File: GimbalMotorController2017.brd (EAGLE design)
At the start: 112.4 x 80 mm, 137 parts, among them J3 APP_2POS_CONFIG5V_HORIZ, Q1 MOSFET-NCHANNELFQP30N06L, Q2 MOSFET-NCHANNELFQP30N06L, Q3 MOSFET-NCHANNELFQP30N06L, Q4 MOSFET-NCHANNELFQP30N06L, Q7 MOSFET-PCHANNEL, Q8 MOSFET-PCHANNEL, Q9 MOSFET-NCHANNELAO3404A, U1 NUP4201MR6, U2 MAX3232D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

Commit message: added CSD18533Q5A fets to Phase B in place of the previously used fets
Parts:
- removed Q3, Q4: MOSFET-NCHANNELFQP30N06L, SparkFun-DiscreteSemi:TO220V
- added U5, U6: CSD18533Q5A, CSD18533:DQJ8
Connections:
- net N$14: now also U6.4; no longer Q3.1
- net N$15: now also U5.4; no longer Q4.1
- net PVDD: now also U6.8; no longer Q3.2
- net SH_B: now also U5.8, U6.3; no longer Q3.3, Q4.2
- net SL_B: now also U5.3; no longer Q4.3
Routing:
- net N$14: track 16.4 -> 12.5 mm
- net N$15: track 10.7 -> 7.85 mm
- net SH_B: track 108.3 -> 106.8 mm
- net GND: track 16.8 -> 15.6 mm
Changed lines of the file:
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@@
 <attribute name="PROD_ID" value="TRANS-10060" x="40.513" y="58.89625" size="1.778" layer="28" rot="MR180" display="off"/>
-</element>
-<element name="Q3" library="SparkFun-DiscreteSemi" package="TO220V" value="MOSFET-NCHANNELFQP30N06L" x="56.388" y="58.89625" smashed="yes" rot="MR180">
-<attribute name="NAME" x="59.944" y="55.46725" size="0.6096" layer="26" ratio="10" rot="MR180"/>
-<attribute name="PROD_ID" value="TRANS-10060" x="56.388" y="58.89625" size="1.778" layer="28" rot="MR180" display="off"/>
-</element>
-<element name="Q4" library="SparkFun-DiscreteSemi" package="TO220V" value="MOSFET-NCHANNELFQP30N06L" x="70.993" y="58.89625" smashed="yes" rot="MR180">
-<attribute name="NAME" x="74.549" y="55.46725" size="0.6096" layer="26" ratio="10" rot="MR180"/>
-<attribute name="PROD_ID" value="TRANS-10060" x="70.993" y="58.89625" size="1.778" layer="28" rot="MR180" display="off"/>
 </element>
 <element name="Q7" library="SparkFun-DiscreteSemi" package="SOT23-3" value="MOSFET-PCHANNEL" x="99.21875" y="43.815" smashed="yes" rot="R270">
@@
 <attribute name="MANUFACTURER_PART_NUMBER" value="CSD18533Q5A" x="-27.94" y="-52.578" size="1.778" layer="27" display="off"/>
 <attribute name="VENDOR" value="Texas Instruments" x="-27.94" y="-52.578" size="1.778" layer="27" display="off"/>
+</element>
+<element name="U5" library="CSD18533" package="DQJ8" value="CSD18533Q5A" x="-27.94" y="-58.674">
+<attribute name="MANUFACTURER_PART_NUMBER" value="CSD18533Q5A" x="-27.94" y="-58.674" size="1.778" layer="27" display="off"/>
+<attribute name="VENDOR" value="Texas Instruments" x="-27.94" y="-58.674" size="1.778" layer="27" display="off"/>
+</element>
+<element name="U6" library="CSD18533" package="DQJ8" value="CSD18533Q5A" x="-27.94" y="-64.77">
+<attribute name="MANUFACTURER_PART_NUMBER" value="CSD18533Q5A" x="-27.94" y="-64.77" size="1.778" layer="27" display="off"/>
+<attribute name="VENDOR" value="Texas Instruments" x="-27.94" y="-64.77" size="1.778" layer="27" display="off"/>
 </element>
 </elements>
@@
 <wire x1="87.4395" y1="66.675" x2="85.88075" y2="66.675" width="0.508" layer="1"/>
 <wire x1="85.88075" y1="66.675" x2="85.852" y2="66.64625" width="0.508" layer="1"/>
-<contactref element="SH1" pad="2"/>
 <contactref element="C24" pad="2"/>
 <contactref element="R18" pad="1"/>
@@
 <via x="45.4025" y="41.62425" extent="1-16" drill="0.381" shape="square"/>
 <wire x1="47.371" y1="62.47765" x2="47.371" y2="63.66175" width="0.3048" layer="16"/>
-<wire x1="77.851" y1="62.47765" x2="77.851" y2="63.66175" width="0.3048" layer="16"/>
 <contactref element="U2" pad="15"/>
 <contactref element="C46" pad="2"/>
@@
 </polygon>
 <contactref element="U4" pad="3"/>
+<contactref element="SH1" pad="2"/>
 <wire x1="108.204" y1="54.61" x2="101.847" y2="63.3095" width="0" layer="19" extent="16-16"/>
 <wire x1="104.66875" y1="47.625" x2="108.204" y2="54.61" width="0" layer="19" extent="1-1"/>
@@
 <wire x1="80.04175" y1="63.0665" x2="84.2645" y2="66.675" width="0" layer="19" extent="16-16"/>
 <wire x1="77.851" y1="63.66175" x2="80.04175" y2="63.0665" width="0" layer="19" extent="16-16"/>
+<wire x1="77.851" y1="62.47765" x2="77.851" y2="63.66175" width="0" layer="19" extent="16-16"/>
 <wire x1="78.74" y1="68.58" x2="77.851" y2="63.66175" width="0" layer="19" extent="16-16"/>
 <wire x1="23.3045" y1="66.675" x2="10.16" y2="76.2" width="0" layer="19" extent="1-1"/>
@@
 <contactref element="Q1" pad="2"/>
 <contactref element="C19" pad="1"/>
-<contactref element="Q3" pad="2"/>
 <contactref element="C22" pad="1"/>
 <contactref element="C25" pad="1"/>
@@
 <contactref element="C37" pad="1"/>
 <contactref element="U3" pad="8"/>
-<wire x1="56.388" y1="58.89625" x2="85.852" y2="63.84625" width="0" layer="19" extent="1-1"/>
-<wire x1="55.372" y1="63.84625" x2="56.388" y2="58.89625" width="0" layer="19" extent="1-1"/>
-<wire x1="62.5585" y1="39.0525" x2="56.388" y2="58.89625" width="0" layer="19" extent="1-1"/>
+<contactref element="U6" pad="8"/>
+<wire x1="55.372" y1="63.84625" x2="85.852" y2="63.84625" width="0" layer="19" extent="1-1"/>
+<wire x1="62.5585" y1="39.0525" x2="55.372" y2="63.84625" width="0" layer="19" extent="1-1"/>
 <wire x1="54.55" y1="18.65" x2="54.55" y2="30.65" width="0" layer="19" extent="1-1"/>
 <wire x1="54.55" y1="17.61775" x2="54.55" y2="18.65" width="0" layer="19" extent="1-1"/>
@@
 <wire x1="22.86" y1="19.812" x2="23.84425" y2="44.73575" width="0" layer="19" extent="1-1"/>
 <wire x1="-25.204928125" y1="-44.577" x2="22.86" y2="19.812" width="0" layer="19" extent="1-1"/>
+<wire x1="-25.204928125" y1="-62.865" x2="-25.204928125" y2="-44.577" width="0" layer="19" extent="1-1"/>
 </signal>
 <signal name="GL_C">
@@
 <signal name="SL_B">
 <contactref element="U$1" pad="39"/>
-<contactref element="Q4" pad="3"/>
 <contactref element="C24" pad="1"/>
 <contactref element="U$1" pad="31"/>
@@
 <wire x1="59.2455" y1="19.14525" x2="59.2455" y2="20.66925" width="0.3048" layer="15"/>
 <contactref element="D10" pad="A"/>
+<contactref element="U5" pad="3"/>
+<wire x1="77.851" y1="60.86175" x2="80.04175" y2="61.2665" width="0" layer="19" extent="16-16"/>
+<wire x1="78.74" y1="57.15" x2="77.851" y2="60.86175" width="0" layer="19" extent="16-16"/>
+<wire x1="74.302" y1="56.388" x2="78.4225" y2="56.8325" width="0" layer="19" extent="16-16"/>
+<wire x1="-30.675071875" y1="-59.309" x2="54.55" y2="19.65" width="0" layer="19" extent="1-1"/>
 </signal>
 <signal name="GL_B">
@@
 <contactref element="C12" pad="2"/>
 <contactref element="U$1" pad="41"/>
-<contactref element="Q3" pad="3"/>
-<contactref element="Q4" pad="2"/>
 <contactref element="R19" pad="1"/>
 <contactref element="U$6" pad="P$1"/>
@@
 <wire x1="60.205" y1="56.1975" x2="60.0145" y2="56.388" width="0.3048" layer="16"/>
 <wire x1="60.0145" y1="56.388" x2="60.0145" y2="57.80975" width="0.3048" layer="16"/>
-<wire x1="60.0145" y1="57.80975" x2="58.928" y2="58.89625" width="0.3048" layer="16"/>
 <wire x1="71.4265" y1="24.59525" x2="71.4265" y2="28.1415" width="0.3048" layer="1"/>
 <wire x1="71.4265" y1="28.1415" x2="68.072" y2="31.496" width="0.3048" layer="1"/>
@@
 <wire x1="50.292" y1="54.61" x2="56.134" y2="54.61" width="0.3048" layer="1"/>
 <wire x1="56.134" y1="54.61" x2="58.674" y2="57.15" width="0.3048" layer="1"/>
+<contactref element="U5" pad="8"/>
+<contactref element="U6" pad="3"/>
+<wire x1="60.0145" y1="57.80975" x2="63.65875" y2="60.706" width="0" layer="19" extent="16-16"/>
+<wire x1="58.674" y1="57.15" x2="60.0145" y2="57.80975" width="0" layer="19" extent="1-16"/>
+<wire x1="-25.204928125" y1="-56.769" x2="54.55" y2="24.65" width="0" layer="19" extent="1-1"/>
+<wire x1="-30.675071875" y1="-65.405" x2="-25.204928125" y2="-56.769" width="0" layer="19" extent="1-1"/>
 </signal>
 <signal name="SL_A">
@@
 </signal>
 <signal name="N$14">
-<contactref element="Q3" pad="1"/>
 <contactref element="R16" pad="1"/>
 <contactref element="D11" pad="C"/>
 <contactref element="U$16" pad="P$1"/>
 <wire x1="53.61475" y1="55.88" x2="53.61475" y2="58.663" width="0.508" layer="16"/>
-<wire x1="53.61475" y1="58.663" x2="53.848" y2="58.89625" width="0.508" layer="16"/>
 <wire x1="57.7145" y1="56.388" x2="56.35625" y2="56.388" width="0.3048" layer="16"/>
-<wire x1="56.35625" y1="56.388" x2="53.848" y2="58.89625" width="0.3048" layer="16"/>
 <wire x1="45.974" y1="54.61" x2="47.244" y2="55.88" width="0.3048" layer="1"/>
 <wire x1="47.244" y1="55.88" x2="52.324" y2="55.88" width="0.3048" layer="1"/>
@@
 <wire x1="52.578" y1="56.134" x2="53.23375" y2="56.134" width="0.3048" layer="16"/>
 <wire x1="53.23375" y1="56.134" x2="53.61475" y2="55.88" width="0.3048" layer="16"/>
+<contactref element="U6" pad="4"/>
+<wire x1="53.61475" y1="55.88" x2="56.35625" y2="56.388" width="0" layer="19" extent="16-16"/>
+<wire x1="-30.675071875" y1="-66.675" x2="45.974" y2="54.61" width="0" layer="19" extent="1-1"/>
 </signal>
 <signal name="N$15">
-<contactref element="Q4" pad="1"/>
 <contactref element="R17" pad="1"/>
 <contactref element="D10" pad="C"/>
@@
 <wire x1="72.002" y1="56.388" x2="71.494" y2="56.896" width="0.508" layer="16"/>
 <wire x1="71.494" y1="56.896" x2="70.45325" y2="56.896" width="0.508" layer="16"/>
-<wire x1="70.45325" y1="56.896" x2="68.453" y2="58.89625" width="0.508" layer="16"/>
 <wire x1="77.089" y1="53.95425" x2="76.43325" y2="54.61" width="0.508" layer="16"/>
 <wire x1="76.43325" y1="54.61" x2="75.184" y2="54.61" width="0.508" layer="16"/>
+<contactref element="U5" pad="4"/>
+<wire x1="-30.675071875" y1="-60.579" x2="70.45325" y2="56.896" width="0" layer="19" extent="1-16"/>
 </signal>
 <signal name="N$17">

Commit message: added CSD18533Q5A fets to Phase A in place of previously used fets. Cleaned up schematic.
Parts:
- removed Q1, Q2: MOSFET-NCHANNELFQP30N06L, SparkFun-DiscreteSemi:TO220V
- added U7, U8: CSD18533Q5A, CSD18533:DQJ8
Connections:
- net N$13: now also U8.4; no longer Q1.1
- net N$16: now also U7.4; no longer Q2.1
- net PVDD: now also U8.8; no longer Q1.2
- net SH_A: now also U7.8, U8.3; no longer Q1.3, Q2.2
- net SL_A: now also U7.3; no longer Q2.3
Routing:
- net SH_A: track 101.6 -> 98.3 mm
- net N$16: track 13.1 -> 10.6 mm
- net GND: track 15.6 -> 14.4 mm
- net N$13: track 7.82 -> 7.01 mm

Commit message: adjusted phase resistor values for 12v to 3.3v voltage divider
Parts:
- R14, R19, R24: value 46.4k -> 13.2k
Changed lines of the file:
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@@
 <element name="R11" library="SparkFun-Passives" package="0805" value="10" x="22.7965" y="54.9275" rot="MR270"/>
 <element name="R12" library="SparkFun-Passives" package="0805" value="10" x="40.16375" y="53.49875" rot="MR180"/>
-<element name="R14" library="SparkFun-Passives" package="0805" value="46.4k" x="56.8325" y="39.0525" smashed="yes" rot="R180">
+<element name="R14" library="SparkFun-Passives" package="0805" value="13.2k" x="56.8325" y="39.0525" smashed="yes" rot="R180">
 <attribute name="NAME" x="57.5945" y="40.513" size="0.6096" layer="25" rot="R180"/>
 <attribute name="VALUE" x="57.8485" y="40.4495" size="0.4064" layer="27" rot="R180"/>
@@
 <attribute name="VALUE" x="78.486" y="54.07025" size="0.4064" layer="28" rot="MR270"/>
 </element>
-<element name="R19" library="SparkFun-Passives" package="0805" value="46.4k" x="52.2605" y="39.0525" smashed="yes">
+<element name="R19" library="SparkFun-Passives" package="0805" value="13.2k" x="52.2605" y="39.0525" smashed="yes">
 <attribute name="NAME" x="52.0065" y="37.592" size="0.6096" layer="25"/>
 <attribute name="VALUE" x="51.2445" y="37.6555" size="0.4064" layer="27"/>
@@
 <attribute name="VALUE" x="28.60675" y="45.847" size="0.4064" layer="27" rot="R270"/>
 </element>
-<element name="R24" library="SparkFun-Passives" package="0805" value="46.4k" x="47.4345" y="39.0525" smashed="yes">
+<element name="R24" library="SparkFun-Passives" package="0805" value="13.2k" x="47.4345" y="39.0525" smashed="yes">
 <attribute name="NAME" x="47.4345" y="37.592" size="0.6096" layer="25"/>
 <attribute name="VALUE" x="46.4185" y="37.6555" size="0.4064" layer="27"/>

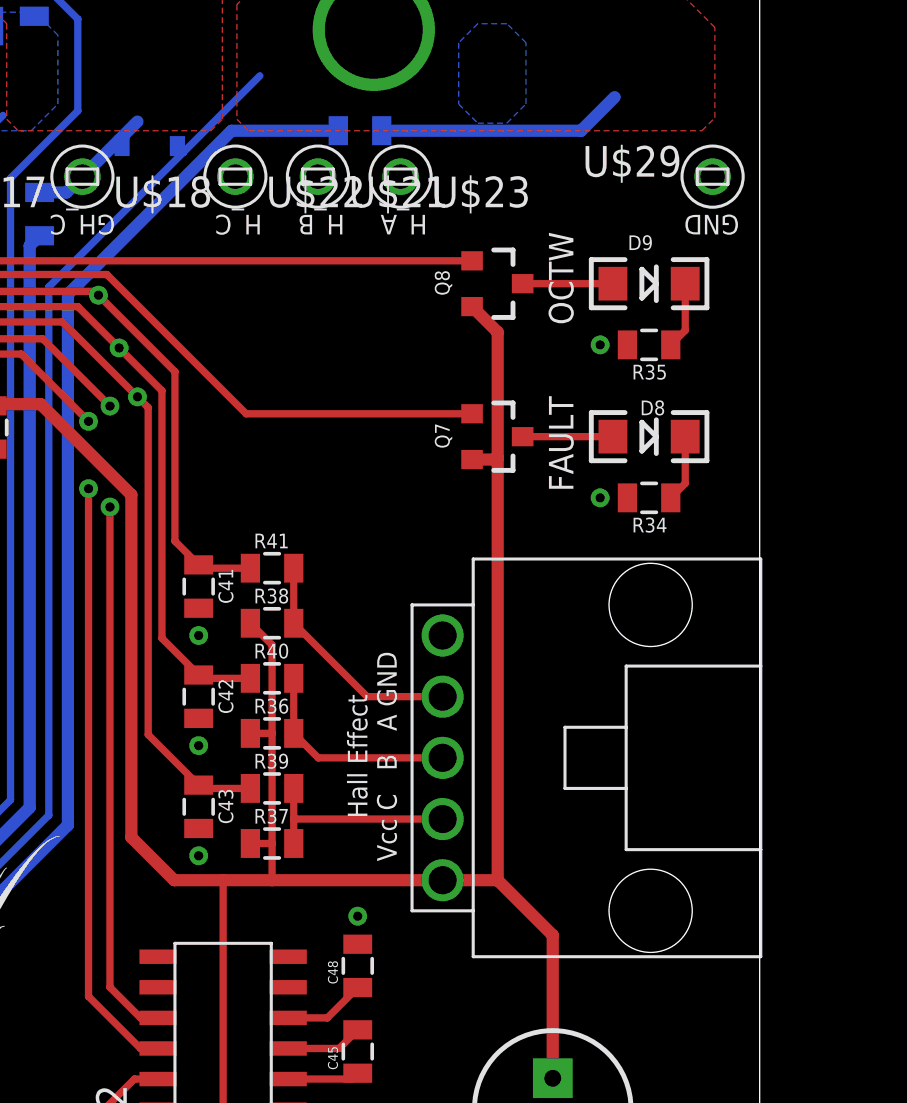
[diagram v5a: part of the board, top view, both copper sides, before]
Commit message: removed hall effect sensor connector
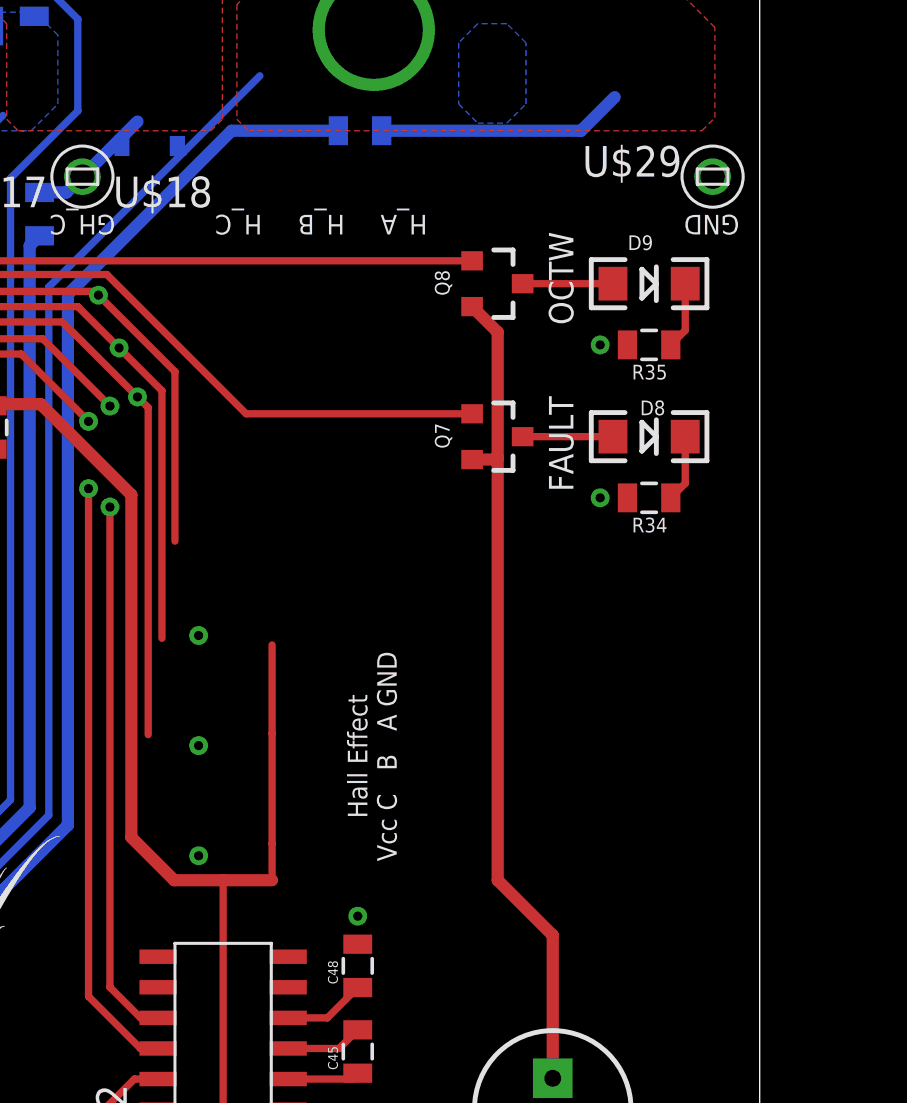
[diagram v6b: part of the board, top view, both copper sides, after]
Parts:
- removed C41, C42, C43: .015u, SparkFun-Passives:0805
- removed R36, R37, R38: 10k, SparkFun-Passives:0805
- removed R39, R40, R41: 10, SparkFun-Passives:0805
- removed U$21, U$22, U$23: TEST_POINT_0.1INDIAM, MRDT-Connectors:TEST_POINT_0.1INDIAM
- removed U$8: 5PIN, Molex-SL:5PIN
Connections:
- removed net N$20: R37.2, R39.2, U$8.2
- removed net N$33: R36.2, R40.2, U$8.3
- removed net N$39: R38.2, R41.2, U$8.4
- net GND: no longer C41.2, C42.2, C43.2, U$8.5
- net HALL_A: no longer C41.1, R41.1, U$22.P$1
- net HALL_B: no longer C42.1, R40.1, U$21.P$1
- net HALL_C: no longer C43.1, R39.1, U$23.P$1
- net VCC: no longer R36.1, R37.1, R38.1, U$8.1
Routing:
- net VCC: track 309.8 -> 297.2 mm
- net N$39: track 9.73 -> 0.00 mm
- net N$33: track 8.89 -> 0.00 mm
- net N$20: track 8.47 -> 0.00 mm
- net HALL_C: track 62.4 -> 54.6 mm
- net HALL_B: track 64.7 -> 58.6 mm
- net HALL_A: track 61.9 -> 57.5 mm
